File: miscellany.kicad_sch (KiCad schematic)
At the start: 12 parts, among them U3 74HC112, U5 74HC123

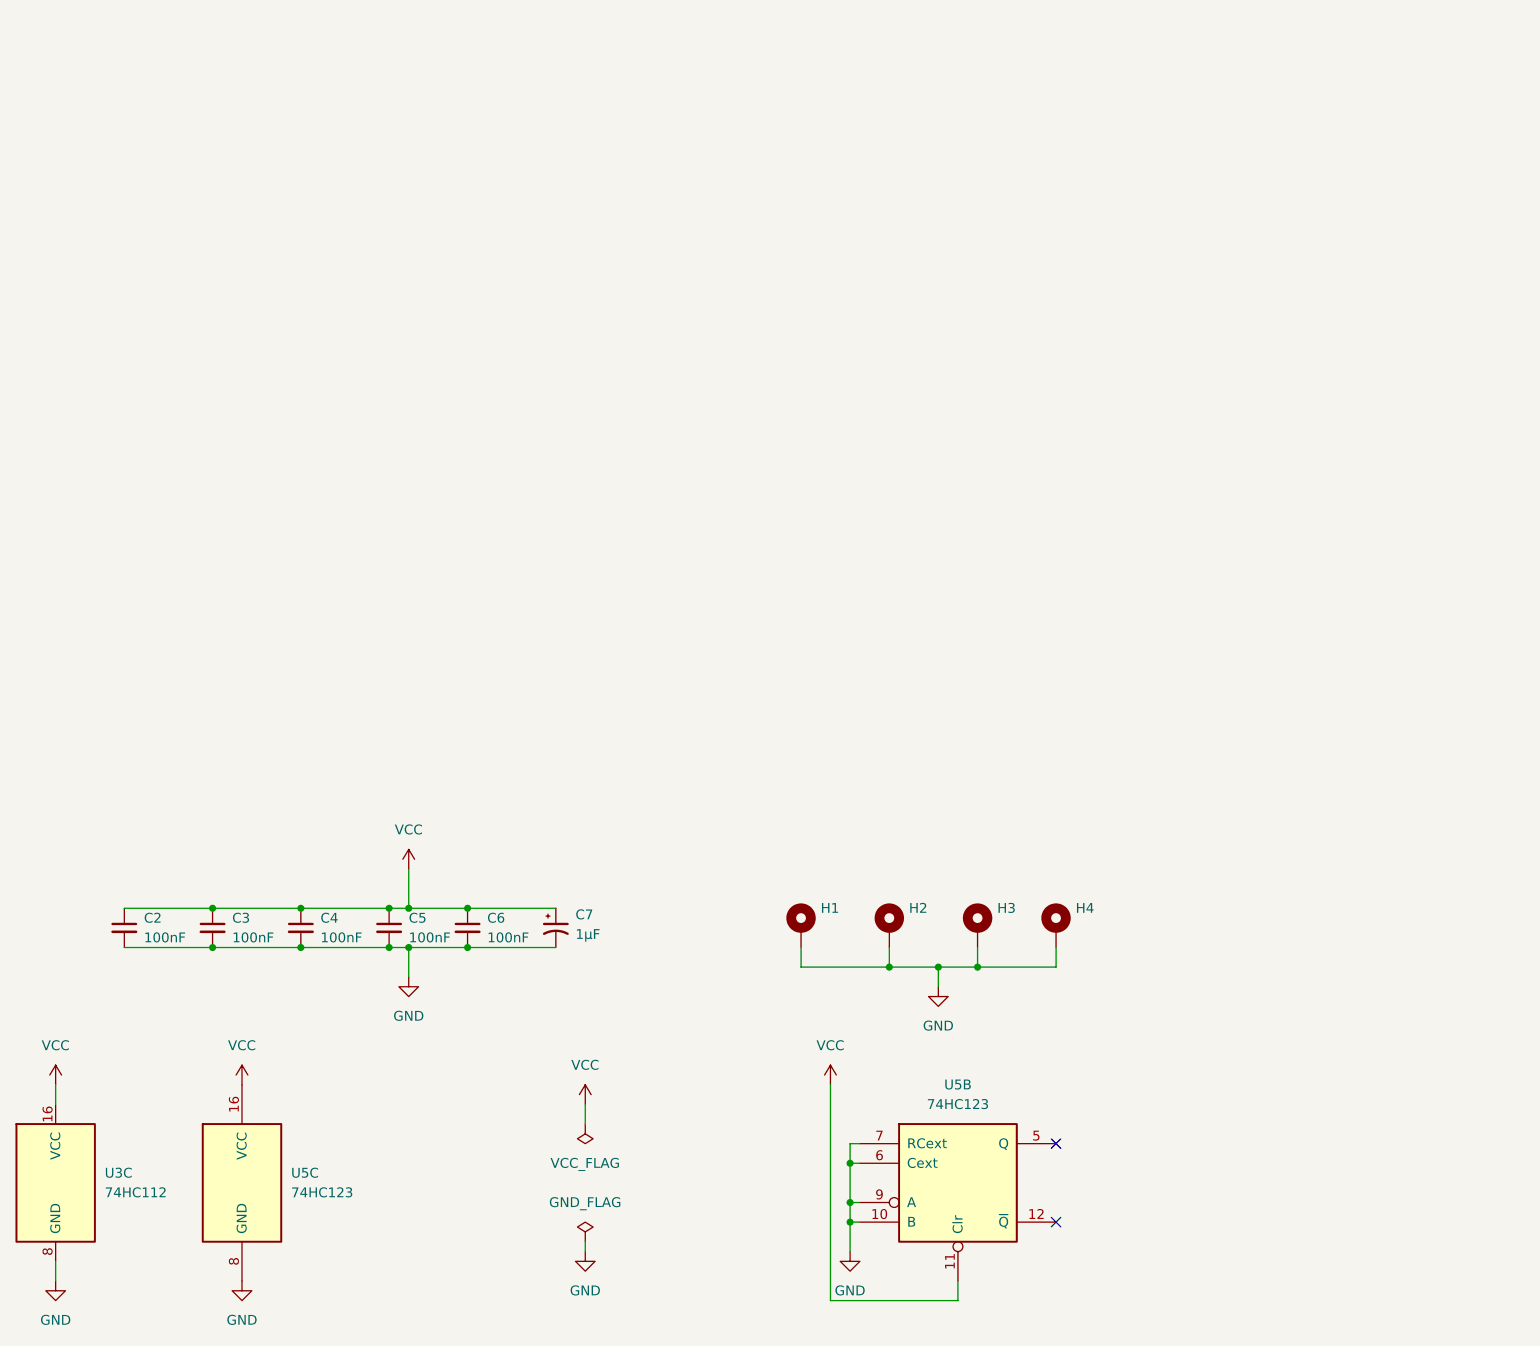
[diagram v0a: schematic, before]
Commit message: Add PAL-2 expansion connection and CS
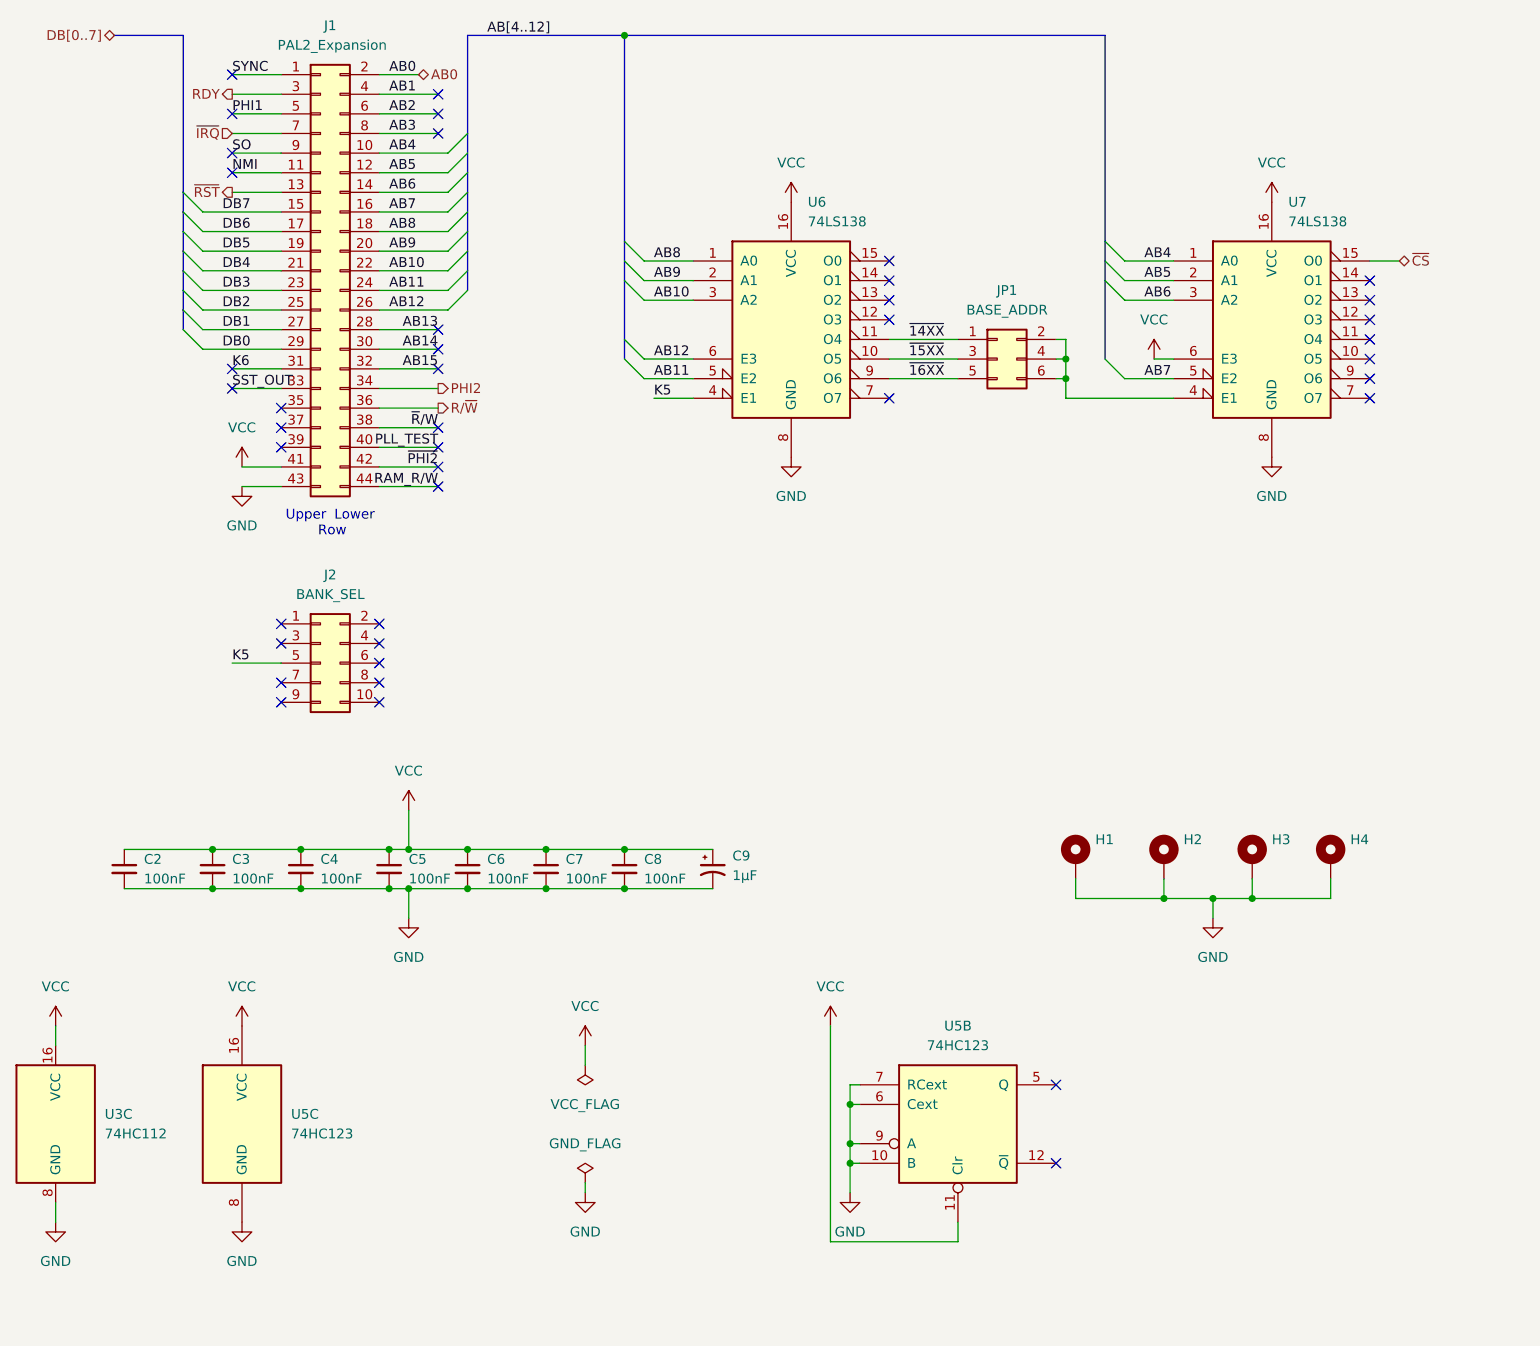
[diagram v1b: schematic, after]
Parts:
- added C7, C8: 100nF, Capacitor_THT:C_Disc_D5.0mm_W2.5mm_P2.50mm, symbol Device:C_Small
- added J1: PAL2_Expansion, Connector_PinHeader_2.54mm:PinHeader_2x22_P2.54mm_Horizontal, symbol Connector_Generic:Conn_02x22_Odd_Even
- added J2: BANK_SEL, Connector_IDC:IDC-Header_2x05_P2.54mm_Horizontal, symbol Connector_Generic:Conn_02x05_Odd_Even
- added JP1: BASE_ADDR, Connector_PinHeader_2.54mm:PinHeader_2x03_P2.54mm_Vertical, symbol Connector_Generic:Conn_02x03_Odd_Even
- added U6, U7: 74LS138, Package_DIP:DIP-16_W7.62mm, symbol 74xx:74LS138
- renumbered C7 to C9
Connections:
- net GND: now also C7.2, C8.2, J1.43 (Pin_43), U6.8 (GND), U7.8 (GND)
- net VCC: now also C7.1, C8.1, J1.41 (Pin_41), U6.16 (VCC), U7.16 (VCC), U7.6 (E3)
- new net: JP1.2 (Pin_2), JP1.4 (Pin_4), JP1.6 (Pin_6), U7.4 (E1)
- new net AB0: J1.2 (Pin_2)
- new net AB1: J1.4 (Pin_4)
- new net AB10: J1.22 (Pin_22), U6.3 (A2)
- new net AB11: J1.24 (Pin_24), U6.5 (E2)
- new net AB12: J1.26 (Pin_26), U6.6 (E3)
- new net AB13: J1.28 (Pin_28)
- new net AB14: J1.30 (Pin_30)
- new net AB15: J1.32 (Pin_32)
- new net AB2: J1.6 (Pin_6)
- new net AB3: J1.8 (Pin_8)
- new net AB4: J1.10 (Pin_10), U7.1 (A0)
- new net AB5: J1.12 (Pin_12), U7.2 (A1)
- new net AB6: J1.14 (Pin_14), U7.3 (A2)
- new net AB7: J1.16 (Pin_16), U7.5 (E2)
- new net AB8: J1.18 (Pin_18), U6.1 (A0)
- new net AB9: J1.20 (Pin_20), U6.2 (A1)
- new net DB0: J1.29 (Pin_29)
- new net DB1: J1.27 (Pin_27)
- new net DB2: J1.25 (Pin_25)
- new net DB3: J1.23 (Pin_23)
- new net DB4: J1.21 (Pin_21)
- new net DB5: J1.19 (Pin_19)
- new net DB6: J1.17 (Pin_17)
- new net DB7: J1.15 (Pin_15)
- new net K5: J2.5 (Pin_5), U6.4 (E1)
- new net K6: J1.31 (Pin_31)
- new net NMI: J1.11 (Pin_11)
- new net PHI1: J1.5 (Pin_5)
- new net PHI2: J1.34 (Pin_34)
- new net PLL_TEST: J1.40 (Pin_40)
- new net RAM_R/W: J1.44 (Pin_44)
- new net RDY: J1.3 (Pin_3)
- new net R/~{W}: J1.36 (Pin_36)
- new net SO: J1.9 (Pin_9)
- new net SST_OUT: J1.33 (Pin_33)
- new net SYNC: J1.1 (Pin_1)
- new net ~{14XX}: JP1.1 (Pin_1), U6.11 (O4)
- new net ~{15XX}: JP1.3 (Pin_3), U6.10 (O5)
- new net ~{16XX}: JP1.5 (Pin_5), U6.9 (O6)
- new net ~{CS}: U7.15 (O0)
- new net ~{IRQ}: J1.7 (Pin_7)
- new net ~{PHI2}: J1.42 (Pin_42)
- new net ~{RST}: J1.13 (Pin_13)
- new net ~{R}/W: J1.38 (Pin_38)
- no-connect marks 2 -> 42
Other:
- note added: "Lower"
- note added: "Row"
- note added: "Upper"
- title: AM9511 Interface for 6509 -> AM9511 Interface for PAL-2
- moved on the sheet: C2, C3, C4, C5, C6, C9, H1, H2, H3, H4, U3C, U5B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

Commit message: Initial PAL-2 version
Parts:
- removed J2: BANK_SEL, Connector_IDC:IDC-Header_2x05_P2.54mm_Horizontal, symbol Connector_Generic:Conn_02x05_Odd_Even
- added C10: 100nF, Capacitor_THT:C_Disc_D5.0mm_W2.5mm_P2.50mm, symbol Device:C_Small
- added J2: K5, Connector_PinHeader_2.54mm:PinHeader_1x01_P2.54mm_Horizontal, symbol Connector:Conn_01x01_Pin
- U3: value 74HC112 -> 74LS112
- U5: value 74HC123 -> 74LS123
- U6, U7: footprint Package_DIP:DIP-16_W7.62mm -> Package_DIP:DIP-16_W7.62mm_Socket
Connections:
- net GND: now also C10.2
- net K5: now also J2.1 (Pin_1)
- net VCC: now also C10.1
- no-connect marks 42 -> 33
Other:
- moved on the sheet: C9
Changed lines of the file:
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@@
 	(title_block
 		(title "AM9511 Interface for PAL-2")
+		(comment 1 "CC BY 4.0")
+		(comment 2 "https://github.com/ceharris/am9511-6502")
+		(comment 3 "This work is based on an original design by Carl E Harris")
 	)
 	(text "Lower"
@@
 	)
 	(junction
+		(at 107.95 144.78)
+		(diameter 0)
+		(color 0 0 0 0)
+	)
+	(junction
 		(at 154.94 78.74)
 		(diameter 0)
@@
 	)
 	(junction
+		(at 107.95 139.7)
+		(diameter 0)
+		(color 0 0 0 0)
+	)
+	(junction
 		(at 154.94 76.2)
 		(diameter 0)
@@
 	)
 	(no_connect
-		(at 53.34 120.65)
-	)
-	(no_connect
 		(at 46.99 52.07)
 	)
 	(no_connect
-		(at 66.04 113.03)
-	)
-	(no_connect
 		(at 132.08 63.5)
 	)
@@
 	)
 	(no_connect
-		(at 66.04 120.65)
-	)
-	(no_connect
 		(at 132.08 66.04)
 	)
 	(no_connect
-		(at 53.34 113.03)
-	)
-	(no_connect
 		(at 194.31 68.58)
 	)
 	(no_connect
-		(at 66.04 118.11)
-	)
-	(no_connect
 		(at 153.67 180.34)
 	)
 	(no_connect
-		(at 66.04 110.49)
-	)
-	(no_connect
 		(at 194.31 71.12)
 	)
@@
 	)
 	(no_connect
-		(at 53.34 110.49)
-	)
-	(no_connect
 		(at 132.08 71.12)
 	)
 	(no_connect
-		(at 53.34 118.11)
-	)
-	(no_connect
 		(at 46.99 49.53)
 	)
 	(no_connect
-		(at 66.04 115.57)
-	)
-	(no_connect
 		(at 194.31 73.66)
 	)
@@
 	(wire
 		(pts
-			(xy 46.99 115.57) (xy 53.34 115.57)
+			(xy 63.5 111.76) (xy 68.58 111.76)
 		)
 		(stroke
@@
 	(wire
 		(pts
+			(xy 107.95 139.7) (xy 120.65 139.7)
+		)
+		(stroke
+			(width 0)
+			(type default)
+		)
+	)
+	(wire
+		(pts
 			(xy 101.6 81.28) (xy 106.68 81.28)
 		)
@@
 	(wire
 		(pts
-			(xy 97.79 144.78) (xy 109.22 144.78)
+			(xy 97.79 144.78) (xy 107.95 144.78)
 		)
 		(stroke
@@
 	(wire
 		(pts
+			(xy 107.95 144.78) (xy 120.65 144.78)
+		)
+		(stroke
+			(width 0)
+			(type default)
+		)
+	)
+	(wire
+		(pts
 			(xy 43.18 62.23) (xy 53.34 62.23)
 		)
@@
 	(wire
 		(pts
-			(xy 97.79 139.7) (xy 109.22 139.7)
+			(xy 97.79 139.7) (xy 107.95 139.7)
 		)
 		(stroke
@@
 		)
 	)
+	(label "K5"
+		(at 68.58 111.76 180)
+		(effects
+			(font
+				(size 1.27 1.27)
+			)
+			(justify right bottom)
+		)
+	)
 	(label "AB4"
 		(at 67.31 49.53 0)
@@
 		)
 	)
-	(label "K5"
-		(at 46.99 115.57 0)
-		(effects
-			(font
-				(size 1.27 1.27)
-			)
-			(justify left bottom)
-		)
-	)
 	(label "AB5"
 		(at 165.1 66.04 0)
@@
 			)
 		)
-		(property "Footprint" "Package_DIP:DIP-16_W7.62mm"
+		(property "Footprint" "Package_DIP:DIP-16_W7.62mm_Socket"
 			(at 119.38 71.12 0)
 			(effects
@@
 	)
 	(symbol
+		(lib_id "Device:C_Small")
+		(at 107.95 142.24 0)
+		(unit 1)
+		(exclude_from_sim no)
+		(in_bom yes)
+		(on_board yes)
+		(dnp no)
+		(fields_autoplaced yes)
+		(property "Reference" "C10"
+			(at 110.49 140.9762 0)
+			(effects
+				(font
+					(size 1.27 1.27)
+				)
+				(justify left)
+			)
+		)
+		(property "Value" "100nF"
+			(at 110.49 143.5162 0)
+			(effects
+				(font
+					(size 1.27 1.27)
+				)
+				(justify left)
+			)
+		)
+		(property "Footprint" "Capacitor_THT:C_Disc_D5.0mm_W2.5mm_P2.50mm"
+			(at 107.95 142.24 0)
+			(effects
+				(font
+					(size 1.27 1.27)
+				)
+				(hide yes)
+			)
+		)
+		(property "Datasheet" "~"
+			(at 107.95 142.24 0)
+			(effects
+				(font
+					(size 1.27 1.27)
+				)
+				(hide yes)
+			)
+		)
+		(property "Description" "Unpolarized capacitor, small symbol"
+			(at 107.95 142.24 0)
+			(effects
+				(font
+					(size 1.27 1.27)
+				)
+				(hide yes)
+			)
+		)
+		(pin "1"
+		)
+		(pin "2"
+		)
+		(instances
+			(project "am9511-6502"
+				(path "/492d2c5d-68ab-43c4-8db3-0d52dc374f84/c9b1cc03-c93e-4f87-a592-e52c2b334e83"
+					(reference "C10")
+					(unit 1)
+				)
+			)
+		)
+	)
+	(symbol
 		(lib_id "am9511-6502-symbols:74HC112")
 		(at 24.13 175.26 0)
@@
 			)
 		)
-		(property "Value" "74HC112"
+		(property "Value" "74LS112"
 			(at 30.48 176.5299 0)
 			(effects
@@
 	(symbol
 		(lib_id "Device:C_Polarized_Small_US")
-		(at 109.22 142.24 0)
+		(at 120.65 142.24 0)
 		(unit 1)
 		(exclude_from_sim no)
@@
 		(fields_autoplaced yes)
 		(property "Reference" "C9"
-			(at 111.76 140.5381 0)
+			(at 123.19 140.5381 0)
 			(effects
 				(font
@@
 		)
 		(property "Value" "1µF"
-			(at 111.76 143.0781 0)
+			(at 123.19 143.0781 0)
 			(effects
 				(font
@@
 		)
 		(property "Footprint" "Capacitor_THT:CP_Radial_D5.0mm_P2.50mm"
-			(at 109.22 142.24 0)
+			(at 120.65 142.24 0)
 			(effects
 				(font
@@
 		)
 		(property "Datasheet" "~"
-			(at 109.22 142.24 0)
+			(at 120.65 142.24 0)
 			(effects
 				(font
@@
 		)
 		(property "Description" "Polarized capacitor, small US symbol"
-			(at 109.22 142.24 0)
+			(at 120.65 142.24 0)
 			(effects
 				(font
@@
 	)
 	(symbol
-		(lib_id "Connector_Generic:Conn_02x05_Odd_Even")
-		(at 58.42 115.57 0)
-		(unit 1)
-		(exclude_from_sim no)
-		(in_bom yes)
-		(on_board yes)
-		(dnp no)
-		(fields_autoplaced yes)
-		(property "Reference" "J2"
-			(at 59.69 104.14 0)
-			(effects
-				(font
-					(size 1.27 1.27)
-				)
-			)
-		)
-		(property "Value" "BANK_SEL"
-			(at 59.69 106.68 0)
-			(effects
-				(font
-					(size 1.27 1.27)
-				)
-			)
-		)
-		(property "Footprint" "Connector_IDC:IDC-Header_2x05_P2.54mm_Horizontal"
-			(at 58.42 115.57 0)
-			(effects
-				(font
-					(size 1.27 1.27)
-				)
-				(hide yes)
-			)
-		)
-		(property "Datasheet" "~"
-			(at 58.42 115.57 0)
-			(effects
-				(font
-					(size 1.27 1.27)
-				)
-				(hide yes)
-			)
-		)
-		(property "Description" ""
-			(at 58.42 115.57 0)
-			(effects
-				(font
-					(size 1.27 1.27)
-				)
-			)
-		)
-		(pin "1"
-		)
-		(pin "10"
-		)
-		(pin "2"
-		)
-		(pin "3"
-		)
-		(pin "4"
-		)
-		(pin "5"
-		)
-		(pin "6"
-		)
-		(pin "7"
-		)
-		(pin "8"
-		)
-		(pin "9"
-		)
-		(instances
-			(project "am9511-6502"
-				(path "/492d2c5d-68ab-43c4-8db3-0d52dc374f84/c9b1cc03-c93e-4f87-a592-e52c2b334e83"
-					(reference "J2")
-					(unit 1)
-				)
-			)
-		)
-	)
-	(symbol
 		(lib_id "Mechanical:MountingHole_Pad")
 		(at 189.23 140.97 0)
@@
 			)
 		)
-		(property "Value" "74HC123"
+		(property "Value" "74LS123"
 			(at 54.61 176.5299 0)
 			(effects
@@
 			)
 		)
-		(property "Datasheet" "https://assets.nexperia.com/documents/data-sheet/74HC_HCT123.pdf"
+		(property "Datasheet" "https://assets.nexperia.com/documents/data-sheet/74LS123.pdf"
 			(at 48.26 175.26 0)
 			(effects
@@
 			)
 		)
-		(property "Value" "74HC123"
+		(property "Value" "74LS123"
 			(at 140.97 165.1 0)
 			(effects
@@
 			)
 		)
-		(property "Datasheet" "https://assets.nexperia.com/documents/data-sheet/74HC_HCT123.pdf"
+		(property "Datasheet" "https://assets.nexperia.com/documents/data-sheet/74LS123.pdf"
 			(at 140.97 175.26 0)
 			(effects
@@
 	)
 	(symbol
+		(lib_id "Connector:Conn_01x01_Pin")
+		(at 58.42 111.76 0)
+		(unit 1)
+		(exclude_from_sim no)
+		(in_bom yes)
+		(on_board yes)
+		(dnp no)
+		(property "Reference" "J2"
+			(at 59.055 106.68 0)
+			(effects
+				(font
+					(size 1.27 1.27)
+				)
+			)
+		)
+		(property "Value" "K5"
+			(at 59.055 109.22 0)
+			(effects
+				(font
+					(size 1.27 1.27)
+				)
+			)
+		)
+		(property "Footprint" "Connector_PinHeader_2.54mm:PinHeader_1x01_P2.54mm_Horizontal"
+			(at 58.42 111.76 0)
+			(effects
+				(font
+					(size 1.27 1.27)
+				)
+				(hide yes)
+			)
+		)
+		(property "Datasheet" "~"
+			(at 58.42 111.76 0)
+			(effects
+				(font
+					(size 1.27 1.27)
+				)
+				(hide yes)
+			)
+		)
+		(property "Description" "Generic connector, single row, 01x01, script generated"
+			(at 58.42 111.76 0)
+			(effects
+				(font
+					(size 1.27 1.27)
+				)
+				(hide yes)
+			)
+		)
+		(pin "1"
+		)
+		(instances
+			(project ""
+				(path "/492d2c5d-68ab-43c4-8db3-0d52dc374f84/c9b1cc03-c93e-4f87-a592-e52c2b334e83"
+					(reference "J2")
+					(unit 1)
+				)
+			)
+		)
+	)
+	(symbol
 		(lib_id "power:GND")
 		(at 69.85 148.59 0)
@@
 			)
 		)
-		(property "Footprint" "Package_DIP:DIP-16_W7.62mm"
+		(property "Footprint" "Package_DIP:DIP-16_W7.62mm_Socket"
 			(at 181.61 71.12 0)
 			(effects

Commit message: Change base address
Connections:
- net ~{CS}: now also U7.13 (O2); no longer U7.15 (O0)
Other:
- note added: "$XX20"
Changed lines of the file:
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@@
+		)
+	)
+	(text "$XX20"
+		(exclude_from_sim no)
+		(at 201.168 67.818 0)
+		(effects
+			(font
+				(size 1.27 1.27)
+			)
 		)
 	)
@@
 	)
 	(no_connect
+		(at 194.31 63.5)
+	)
+	(no_connect
 		(at 132.08 68.58)
 	)
@@
 	(no_connect
 		(at 132.08 66.04)
-	)
-	(no_connect
-		(at 194.31 68.58)
 	)
 	(no_connect
@@
 	(wire
 		(pts
+			(xy 194.31 68.58) (xy 205.74 68.58)
+		)
+		(stroke
+			(width 0)
+			(type default)
+		)
+	)
+	(wire
+		(pts
 			(xy 46.99 41.91) (xy 53.34 41.91)
 		)
@@
 		(pts
 			(xy 74.93 69.85) (xy 66.04 69.85)
-		)
-		(stroke
-			(width 0)
-			(type default)
-		)
-	)
-	(wire
-		(pts
-			(xy 194.31 63.5) (xy 198.12 63.5)
 		)
 		(stroke
@@
 	(hierarchical_label "~{CS}"
 		(shape bidirectional)
-		(at 198.12 63.5 0)
-		(effects
-			(font
+		(at 205.74 68.58 0)
+		(effects
+			(font

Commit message: Minor improvements
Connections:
- net K5: now also J1.35 (Pin_35)
- no-connect marks 33 -> 32
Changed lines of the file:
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@@
-	)
-	(no_connect
-		(at 53.34 82.55)
 	)
 	(no_connect
@@
 	(wire
 		(pts
+			(xy 46.99 82.55) (xy 53.34 82.55)
+		)
+		(stroke
+			(width 0)
+			(type default)
+		)
+	)
+	(wire
+		(pts
 			(xy 46.99 41.91) (xy 53.34 41.91)
 		)
@@
 		(effects
 			(font
+				(size 1.27 1.27)
+			)
+			(justify left bottom)
+		)
+	)
+	(label "K5"
+		(at 46.99 82.55 0)
+		(effects
+			(font
